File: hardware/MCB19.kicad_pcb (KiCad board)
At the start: 2 copper layers, 204 x 81.5 mm, 109 parts, among them J401 USART, J402 DISABLE, J601 RJ45, J602 RJ45, J611 +BAT_IN, J612 -BAT_IN, J613 +BAT_OUT, J614 -BAT_OUT, Q601 IRFP260N, Q602 IRFP260N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

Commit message: enable, vi, vo
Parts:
- added Q603: BC857, Package_TO_SOT_SMD:SOT-23, F.Cu at (93.6, 146.0)
- added Q604: BC847, Package_TO_SOT_SMD:SOT-23, F.Cu at (97.7, 147.9)
- added R611: 1k, Resistor_SMD:R_0805_2012Metric_Pad1.15x1.40mm_HandSolder, F.Cu at (97.6, 151.3)
- added R612: 1k, Resistor_SMD:R_0805_2012Metric_Pad1.15x1.40mm_HandSolder, F.Cu at (93.5, 151.4)
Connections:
- D601 pad 2: +15V -> Net-(D601-Pad2)
- J601 pad 9: GND -> (no net)
- J602 pad 9: GND -> (no net)
- U601 pad 1: +15V -> Net-(D601-Pad2)
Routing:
- net Net-(D601-Pad2): track 0.00 -> 5.58 mm, vias 0 -> 1
- net GND: track 558.8 -> 563.0 mm, vias 17 -> 18
- net Net-(Q603-Pad1): track 0.00 -> 3.06 mm
- net Net-(Q604-Pad2): track 0.00 -> 2.41 mm
- net +15V: track 158.4 -> 160.6 mm, vias 1 -> 2
- net (no net): track 0.00 -> 1.82 mm, vias 0 -> 1

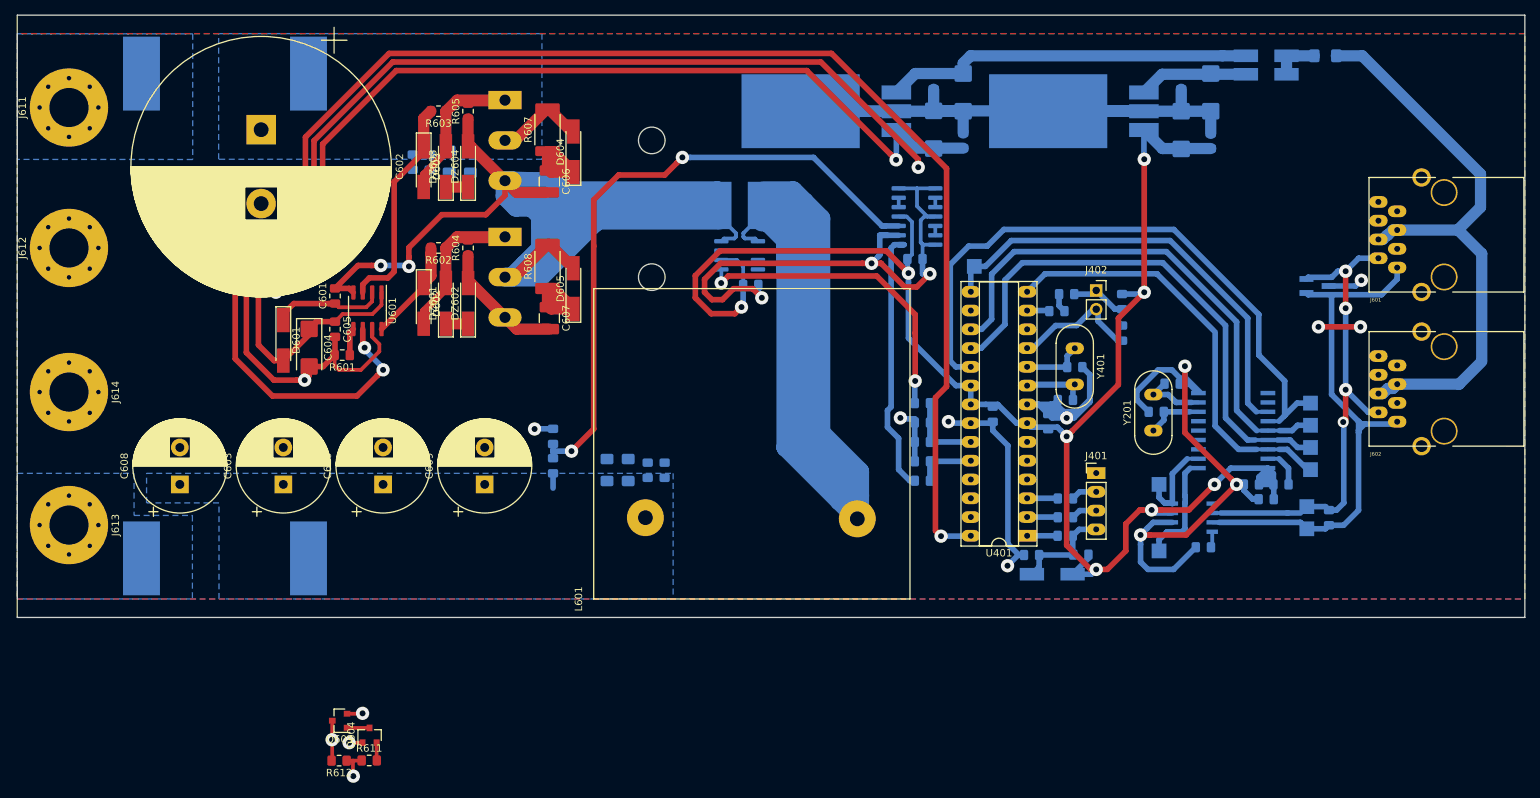
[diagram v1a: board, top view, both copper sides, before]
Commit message: Adição das mudanças pré-DSB(SF) feitas no MCB19
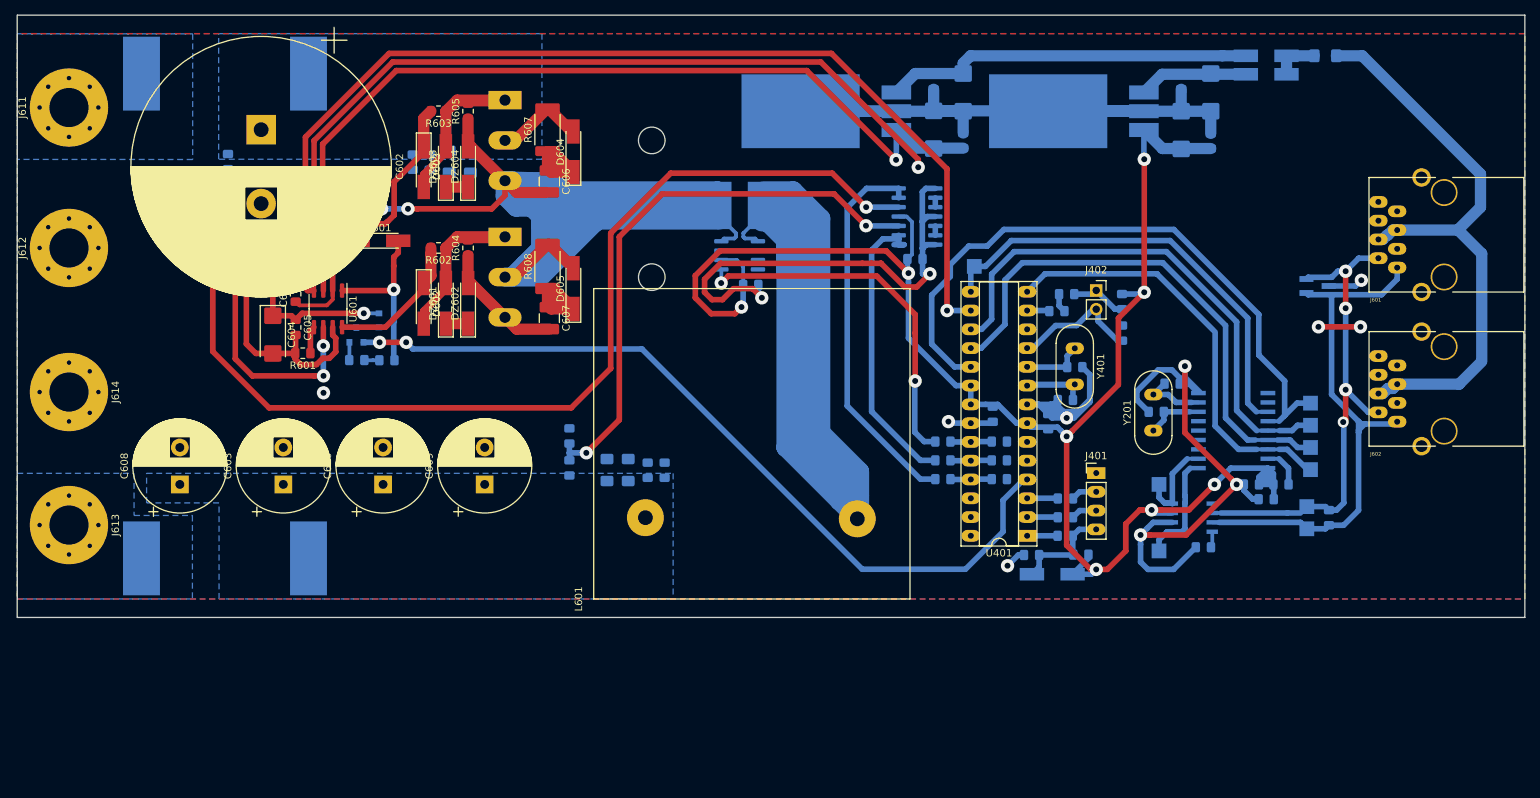
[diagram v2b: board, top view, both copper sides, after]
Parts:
- added C409: 100nF, Capacitor_SMD:C_0805_2012Metric_Pad1.15x1.40mm_HandSolder, B.Cu at (182.9, 113.3)
- added R613: 15k, Resistor_SMD:R_0805_2012Metric_Pad1.15x1.40mm_HandSolder, B.Cu at (78.5, 70.3)
- added R614: 1k2, Resistor_SMD:R_0805_2012Metric_Pad1.15x1.40mm_HandSolder, B.Cu at (78.5, 74.6)
- C407: value 100n -> 100nF
- Q603, Q604, R611, R612: moved to B.Cu
- R407, R408: value 1k5 -> 680
- R409: value 6k8 -> 680
- R609: value 470R -> 15k
- R610: value 1k5 -> 1k2
- moved R612 54.6 mm to (100.0, 97.2), turned to 0 degrees
- moved Q603 54.5 mm to (99.9, 91.8), turned to 0 degrees
- moved Q604 54.2 mm to (95.9, 93.8)
- moved R611 54.2 mm to (95.9, 97.2), turned to 180 degrees
- moved D601 18.6 mm to (98.8, 81.0), turned to 0 degrees
- moved C408 10.4 mm to (182.9, 110.7), turned to 0 degrees
- moved C407 10.4 mm to (182.9, 108.2), turned to 180 degrees
- moved R409 8.15 mm to (175.3, 113.3), turned to 180 degrees
- moved R407 5.90 mm to (175.3, 108.2)
- moved C601 5.34 mm to (87.7, 88.2)
- moved C605 5.34 mm to (87.7, 92.7)
- moved U601 5.34 mm to (92.1, 90.2)
- moved R601 5.34 mm to (88.6, 96.2)
- moved C604 5.23 mm to (84.6, 93.7)
- moved R609 4.80 mm to (124.7, 111.8)
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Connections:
- Q604 pad 1: (no net) -> /MCU/ENABLE
- R409 pad 1: GND -> Net-(C409-Pad1)
- R409 pad 2: Net-(C407-Pad2) -> /driver/LM324B
- R609 pad 1: GND -> Net-(R609-Pad1)
- R609 pad 2: Net-(R609-Pad2) -> Net-(C603-Pad1)
- R610 pad 1: Net-(C603-Pad1) -> GND
- R610 pad 2: Net-(R609-Pad2) -> Net-(R609-Pad1)
- U201 pad 5: (no net) -> Net-(U201-Pad5)
- U202 pad 10: (no net) -> Net-(U202-Pad10)
- U202 pad 11: (no net) -> Net-(U202-Pad11)
- U202 pad 3: (no net) -> Net-(U202-Pad3)
- U202 pad 4: (no net) -> Net-(U202-Pad4)
- U202 pad 5: (no net) -> Net-(U202-Pad5)
- U202 pad 6: (no net) -> Net-(U202-Pad6)
- U401 pad 12: (no net) -> Net-(U401-Pad12)
- U401 pad 16: (no net) -> /MCU/PWM
- U401 pad 25: (no net) -> Net-(C409-Pad1)
- U401 pad 26: (no net) -> Net-(U401-Pad26)
- U401 pad 27: (no net) -> Net-(U401-Pad27)
- U401 pad 28: /MCU/PWM -> Net-(U401-Pad28)
- U401 pad 4: (no net) -> /MCU/ENABLE
- U401 pad 5: (no net) -> Net-(U401-Pad5)
- U401 pad 6: (no net) -> Net-(U401-Pad6)
- U603 pad 2: GND -> /driver/LM324A
- U603 pad 3: Net-(R609-Pad2) -> Net-(R609-Pad1)
- U603 pad 5: Net-(U603-Pad5) -> Net-(R613-Pad1)
- U603 pad 6: Net-(U603-Pad5) -> /driver/LM324B
- U603 pad 7: GND -> /driver/LM324B
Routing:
- net Net-(R613-Pad1): track 0.00 -> 149.7 mm, vias 0 -> 2
- net /MCU/ENABLE: track 0.00 -> 110.1 mm, vias 0 -> 2
- net Net-(R609-Pad2): track 89.4 -> 0.00 mm, vias 2 -> 0
- net Net-(R609-Pad1): track 0.00 -> 77.6 mm, vias 0 -> 2
- net GND: track 563.0 -> 506.1 mm, vias 18 -> 13
- net /driver/LM324B: track 0.00 -> 52.2 mm
- net /MCU/PWM: track 217.1 -> 174.1 mm
- net Net-(D601-Pad2): track 5.58 -> 23.5 mm
- net +15V: track 160.6 -> 145.8 mm
- net /MCU/INALLL: track 42.7 -> 49.9 mm
- net Net-(C601-Pad2): track 253.7 -> 259.7 mm
- net Net-(C409-Pad1): track 0.00 -> 5.63 mm
- net Net-(D602-Pad1): track 13.7 -> 19.1 mm
- net Net-(C407-Pad2): track 10.8 -> 5.63 mm
- net /driver/LM324A: track 36.3 -> 40.8 mm
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
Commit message: small fixes in layout. Fabrication files exported.
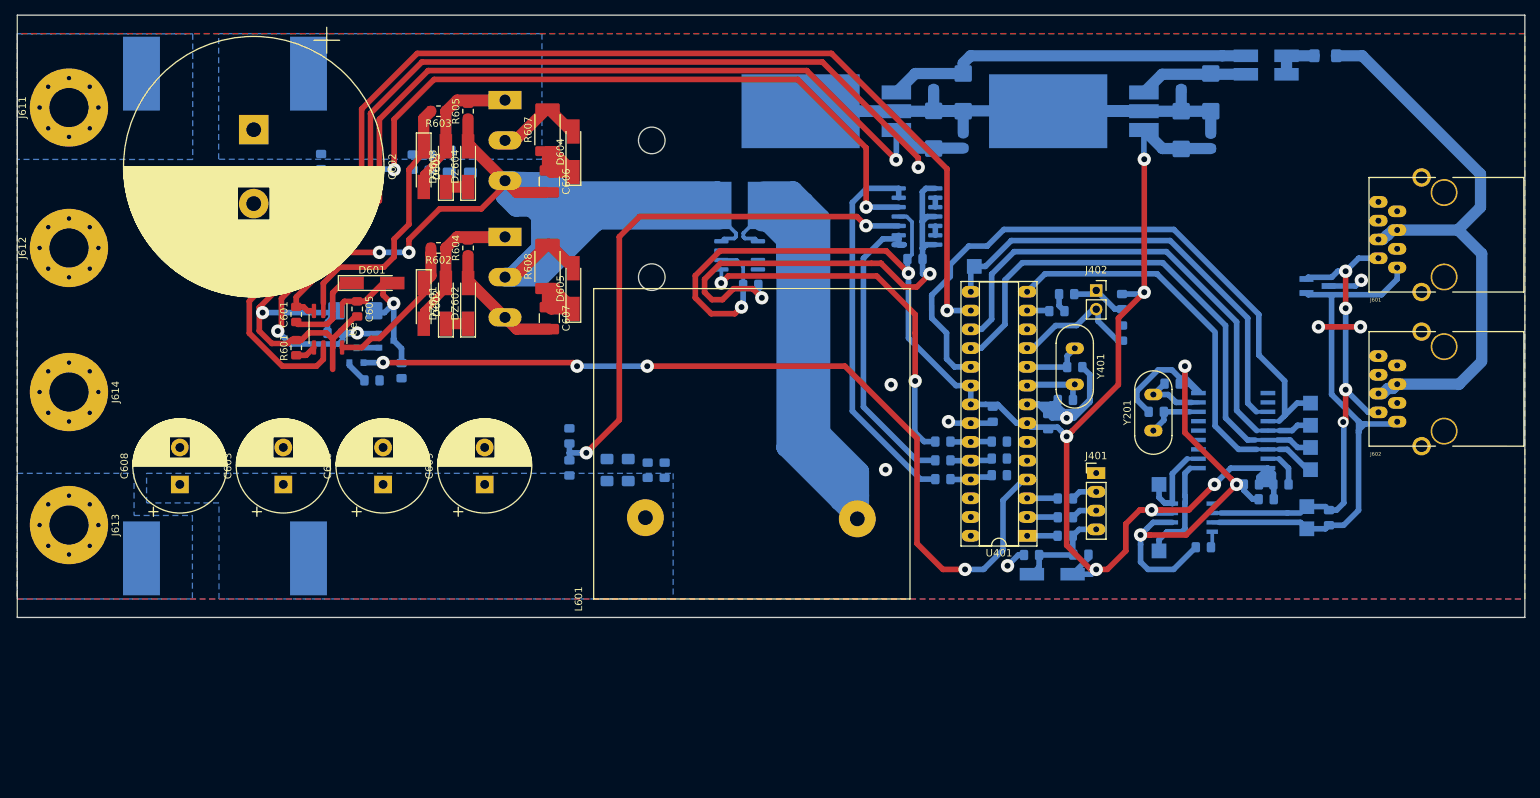
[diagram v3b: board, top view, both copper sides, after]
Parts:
- added C621: 100nF, Capacitor_SMD:C_0805_2012Metric_Pad1.15x1.40mm_HandSolder, B.Cu at (93.0, 93.5)
- C604: moved to B.Cu
- moved R613 12.6 mm to (91.1, 70.3)
- moved R614 12.6 mm to (91.1, 74.6)
- moved C604 11.6 mm to (95.8, 90.5), turned to 180 degrees
- moved C605 8.70 mm to (96.0, 90.2)
- moved D601 5.78 mm to (98.0, 86.8)
- moved R611 3.43 mm to (98.0, 99.9)
- moved C601 2.76 mm to (87.8, 91.0)
- moved Q603 2.75 mm to (99.9, 94.5)
- moved Q604 2.75 mm to (95.9, 96.5)
- moved Ue 2.75 mm to (92.1, 93.0)
- moved R612 2.43 mm to (102.0, 98.6), turned to 90 degrees
- moved R601 1.16 mm to (87.8, 95.5), turned to 90 degrees
- moved C602 1.00 mm to (82.0, 66.0)
- moved C409 0.53 mm to (182.9, 112.8)
- moved C408 0.24 mm to (182.9, 110.5)
- renumbered U601 to Ue
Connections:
- C604 pad 1: +15V -> Net-(C604-Pad1)
- C605 pad 1: +15V -> Net-(C604-Pad1)
- D601 pad 2: Net-(D601-Pad2) -> Net-(C604-Pad1)
- Q603 pad 3: Net-(D601-Pad2) -> Net-(C604-Pad1)
- R612 pad 2: Net-(D601-Pad2) -> Net-(C604-Pad1)
- U201 pad 5: Net-(U201-Pad5) -> (no net)
- U202 pad 10: Net-(U202-Pad10) -> (no net)
- U202 pad 11: Net-(U202-Pad11) -> (no net)
- U202 pad 3: Net-(U202-Pad3) -> (no net)
- U202 pad 4: Net-(U202-Pad4) -> (no net)
- U202 pad 5: Net-(U202-Pad5) -> (no net)
- U202 pad 6: Net-(U202-Pad6) -> (no net)
- U401 pad 12: Net-(U401-Pad12) -> (no net)
- U401 pad 26: Net-(U401-Pad26) -> (no net)
- U401 pad 27: Net-(U401-Pad27) -> (no net)
- U401 pad 28: Net-(U401-Pad28) -> (no net)
- U401 pad 5: Net-(U401-Pad5) -> (no net)
- U401 pad 6: Net-(U401-Pad6) -> (no net)
- Ue pad 1: Net-(D601-Pad2) -> Net-(C604-Pad1)
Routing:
- net Net-(R613-Pad1): track 149.7 -> 101.3 mm
- net Net-(D601-Pad2): track 23.5 -> 0.00 mm, vias 1 -> 0
- net Net-(C604-Pad1): track 0.00 -> 22.9 mm, vias 0 -> 1
- net /MCU/PWM: track 174.1 -> 161.7 mm, vias 3 -> 1
- net /MCU/ENABLE: track 110.1 -> 119.1 mm, vias 2 -> 4
- net GND: track 506.1 -> 512.2 mm, vias 13 -> 15
- net Net-(C601-Pad1): track 16.3 -> 10.8 mm
- net Net-(Q603-Pad1): track 3.06 -> 6.12 mm
- net Net-(D603-Pad1): track 34.4 -> 37.0 mm
- net Net-(R609-Pad1): track 77.6 -> 75.1 mm
- net +15V: track 145.8 -> 148.0 mm, vias 2 -> 3
- net Net-(D602-Pad1): track 19.1 -> 20.7 mm
- net /driver/LM324A: track 40.8 -> 42.0 mm
- net Net-(R601-Pad1): track 3.72 -> 2.83 mm
- net Net-(Q604-Pad2): track 2.41 -> 3.24 mm
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
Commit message: driver better referenced to low-side mosfet
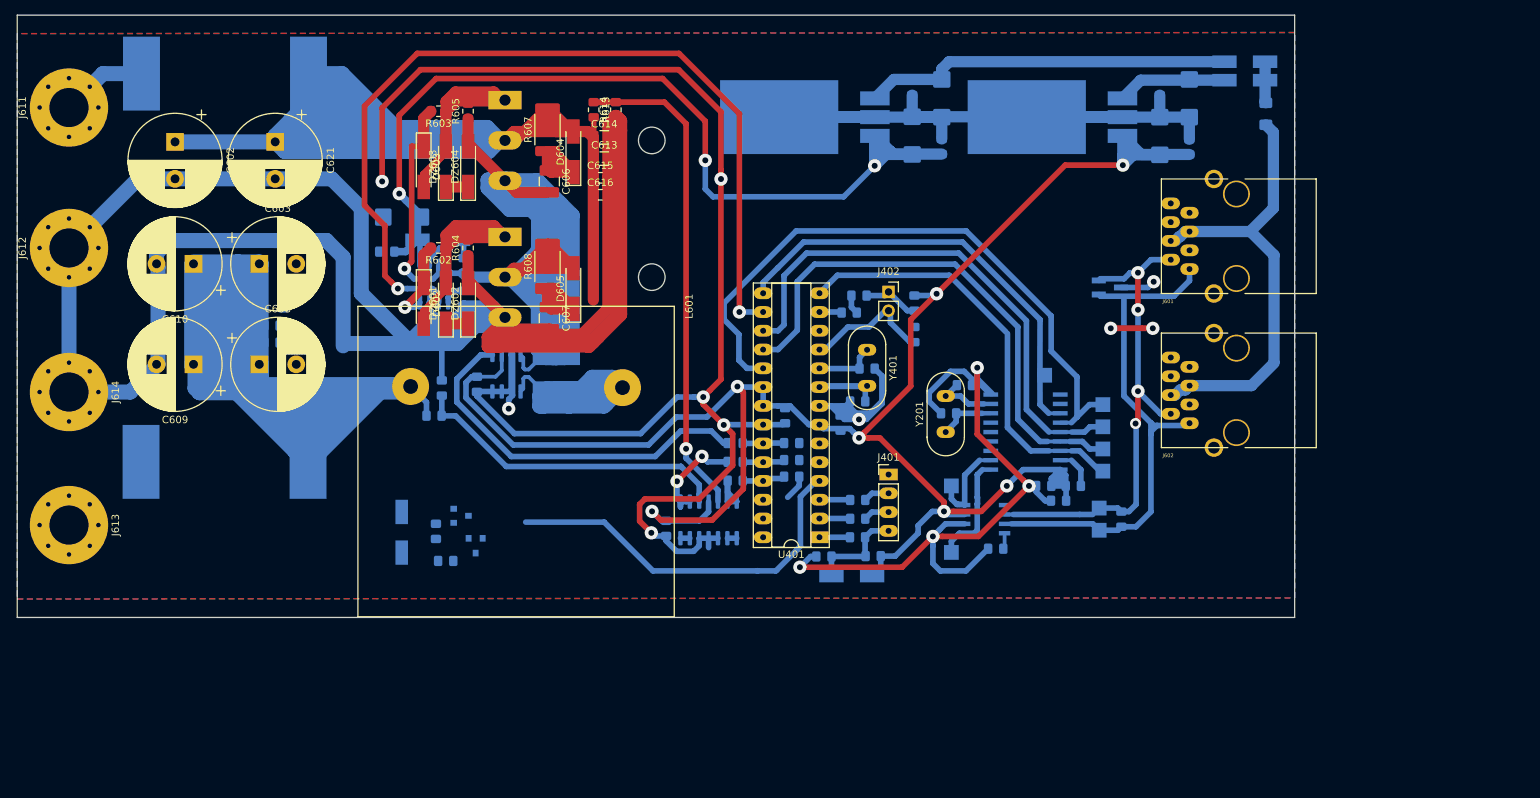
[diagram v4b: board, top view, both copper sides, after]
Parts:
- added D606: ES2A, Diode_SMD:D_MiniMELF_Handsoldering, B.Cu at (102.0, 120.5)
- C601, C605, D601, R601: moved to B.Cu
- C602: footprint Capacitor_THT:CP_Radial_D35.0mm_P10.00mm_SnapIn -> Capacitor_THT:CP_Radial_D12.5mm_P5.00mm
- C613, C614, C615, C616, R613, R614: moved to F.Cu
- C621: value 100nF -> 4700uF; footprint Capacitor_SMD:C_0805_2012Metric_Pad1.15x1.40mm_HandSolder -> Capacitor_THT:CP_Radial_D12.5mm_P5.00mm; moved to F.Cu
- U501: value LM7815 -> LM7812
- U601: renamed from Ue; moved to B.Cu
- moved C619 55.9 mm to (84.5, 94.8), turned to 0 degrees
- moved C620 54.5 mm to (84.5, 92.5), turned to 0 degrees
- moved C617 53.0 mm to (84.5, 89.9), turned to 0 degrees
- moved C618 51.8 mm to (84.5, 87.0), turned to 0 degrees
- moved U603 49.8 mm to (143.6, 118.8), turned to 270 degrees
- moved C612 49.6 mm to (137.8, 120.0), turned to 90 degrees
- moved C609 42.6 mm to (73.8, 97.8), turned to 180 degrees
- moved R614 41.5 mm to (131.0, 63.3)
- moved L601 41.1 mm to (138.9, 89.9), turned to 270 degrees
- moved C611 39.4 mm to (112.2, 100.5), turned to 90 degrees
- moved C610 39.4 mm to (73.8, 84.2), turned to 180 degrees
- moved R613 37.5 mm to (128.0, 63.3), turned to 270 degrees
- moved U602 35.4 mm to (116.2, 99.0), turned to 90 degrees
- moved R606 33.6 mm to (123.0, 99.0), turned to 180 degrees
- moved Q603 30.3 mm to (112.0, 122.3), turned to 270 degrees
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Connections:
- C503 pad 1: +15V -> +12V
- C504 pad 1: +15V -> +12V
- C604 pad 1: Net-(C604-Pad1) -> +12V
- C605 pad 1: Net-(C604-Pad1) -> +12V
- C621 pad 1: +15V -> +BATT
- D601 pad 2: Net-(C604-Pad1) -> +12V
- F602 pad 1: Net-(F602-Pad1) -> (no net)
- J613 pad 1: Net-(F602-Pad1) -> Net-(J613-Pad1)
- L601 pad 1: Net-(C603-Pad1) -> Net-(L601-Pad1)
- L601 pad 2: Net-(L601-Pad2) -> Net-(C603-Pad1)
- Q603 pad 2: +15V -> (no net)
- Q603 pad 3: Net-(C604-Pad1) -> /driver/relay_coil
- R606 pad 1: Net-(L601-Pad2) -> Net-(L601-Pad1)
- R612 pad 2: Net-(C604-Pad1) -> /driver/relay_coil
- U501 pad 3: +15V -> +12V
- U601 pad 1: Net-(C604-Pad1) -> +12V
- U602 pad 1: Net-(L601-Pad2) -> Net-(L601-Pad1)
- U603 pad 10: Net-(U603-Pad10) -> GND
- U603 pad 12: Net-(U603-Pad12) -> GND
- U603 pad 13: Net-(U603-Pad12) -> Net-(U603-Pad13)
- U603 pad 14: GND -> Net-(U603-Pad13)
- U603 pad 8: GND -> Net-(U603-Pad8)
- U603 pad 9: Net-(U603-Pad10) -> Net-(U603-Pad8)
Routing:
- net GND: track 512.2 -> 914.6 mm, vias 15 -> 14
- net Net-(C603-Pad1): track 0.00 -> 352.3 mm
- net +BATT: track 11.9 -> 298.2 mm
- net Net-(L601-Pad2): track 192.2 -> 0.00 mm
- net +15V: track 148.0 -> 0.00 mm, vias 3 -> 0
- net +12V: track 0.00 -> 135.7 mm, vias 0 -> 3
- net /MCU/ENABLE: track 119.1 -> 51.8 mm, vias 4 -> 0
- net Net-(L601-Pad1): track 0.00 -> 64.2 mm
- net /driver/LM324B: track 51.6 -> 7.48 mm
- net /MCU/PWM: track 161.7 -> 120.6 mm, vias 1 -> 2
- net Net-(R613-Pad1): track 101.3 -> 66.6 mm, vias 2 -> 1
- net +5V: track 230.4 -> 263.6 mm, vias 8 -> 7
- net Net-(R609-Pad1): track 75.1 -> 43.6 mm, vias 2 -> 0
- net /driver/LM324A: track 42.0 -> 14.8 mm, vias 0 -> 2
- net /CANBUS CONN/CAN_18V: track 93.8 -> 70.6 mm
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- removed copper zone on B.Cu, net +BATT
- removed copper zone on B.Cu, net Net-(C603-Pad1)
- removed copper zone on B.Cu, net Net-(F601-Pad2)
- removed copper zone on B.Cu, net Net-(F602-Pad1)
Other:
- board size 204 x 81.5 mm -> 172.8 x 81.5 mm

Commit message: relay driver almost finished
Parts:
- added K601: G5LE-1, Relay_THT:Relay_SPDT_Omron-G5LE-1, B.Cu at (97.2, 123.2)
- added R1: 90R, Resistor_SMD:R_0805_2012Metric_Pad1.15x1.40mm_HandSolder, B.Cu at (104.8, 127.0)
- moved F602 22.9 mm to (89.5, 109.2), turned to 180 degrees
- moved Q603 6.23 mm to (108.0, 127.0), turned to 180 degrees
- moved Q604 4.36 mm to (112.4, 121.9), turned to 90 degrees
- moved R612 4.23 mm to (104.1, 122.6), turned to 270 degrees
- moved D606 2.72 mm to (102.0, 123.2)
- moved R611 1.58 mm to (105.4, 119.4), turned to 0 degrees
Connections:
- F501 pad 2: /CANBUS CONN/CAN_18V -> VCC
- F602 pad 1: (no net) -> Net-(F602-Pad1)
- J601 pad 4: /CANBUS CONN/CAN_18V -> VCC
- J601 pad 5: /CANBUS CONN/CAN_18V -> VCC
- J602 pad 4: /CANBUS CONN/CAN_18V -> VCC
- J602 pad 5: /CANBUS CONN/CAN_18V -> VCC
- Q603 pad 2: (no net) -> VCC
- Q603 pad 3: /driver/relay_coil -> Net-(Q603-Pad3)
- U201 pad 5: (no net) -> Net-(U201-Pad5)
- U202 pad 10: (no net) -> Net-(U202-Pad10)
- U202 pad 11: (no net) -> Net-(U202-Pad11)
- U202 pad 3: (no net) -> Net-(U202-Pad3)
- U202 pad 4: (no net) -> Net-(U202-Pad4)
- U202 pad 5: (no net) -> Net-(U202-Pad5)
- U202 pad 6: (no net) -> Net-(U202-Pad6)
- U401 pad 12: (no net) -> Net-(U401-Pad12)
- U401 pad 26: (no net) -> Net-(U401-Pad26)
- U401 pad 27: (no net) -> Net-(U401-Pad27)
- U401 pad 28: (no net) -> Net-(U401-Pad28)
- U401 pad 5: (no net) -> Net-(U401-Pad5)
- U401 pad 6: (no net) -> Net-(U401-Pad6)
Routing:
- net Net-(C603-Pad1): track 352.3 -> 249.2 mm
- net VCC: track 0.00 -> 70.6 mm
- net /CANBUS CONN/CAN_18V: track 70.6 -> 0.00 mm
- net GND: track 914.6 -> 926.0 mm
- added copper zone on B.Cu, net Net-(C603-Pad1)
